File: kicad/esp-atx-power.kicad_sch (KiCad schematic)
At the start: 43 parts, among them J101 Conn_02x02_Odd_Even, J102 Conn_02x02_Odd_Even, J103 Conn_02x02_Odd_Even, J104 Conn_02x02_Odd_Even, J105 GT-USB-7010ASV, K101 G3VM-61D1, K102 G3VM-61D1, K103 G3VM-61D1, K104 G3VM-61D1, Q101 SS8050, Q102 SS8050, SW101 TS-1187A-B-A-B, SW102 TS-1187A-B-A-B, U102 LD1117S33CTR, U103 USBLC6-2P6, U104 CP2102-GMR

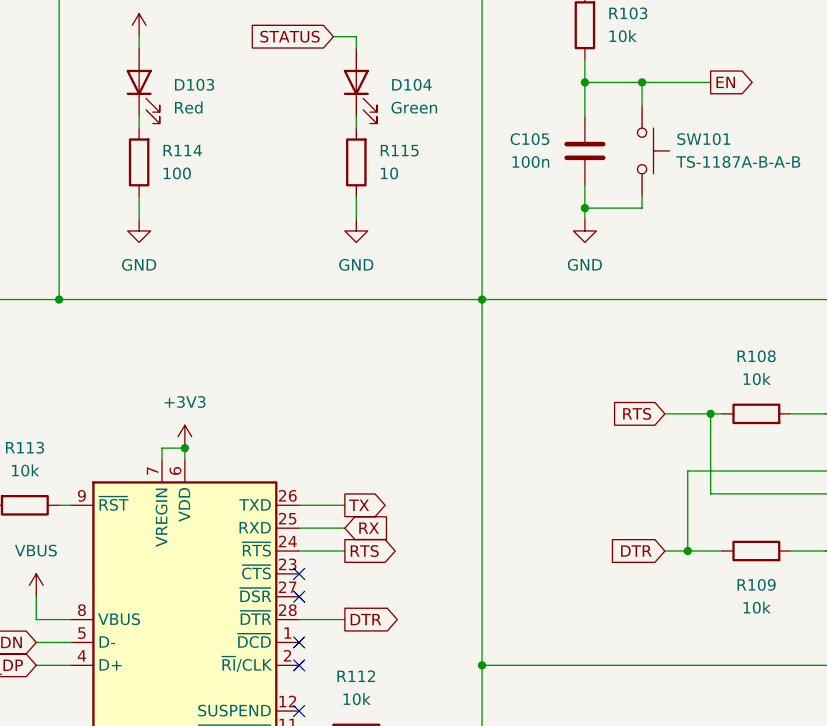
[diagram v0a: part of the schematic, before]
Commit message: Fix RTS/DTR and increase LEDs resistors
- RTS/DTR has been inverted and RTS assertin doesn't reset the board.
- Increase the LED resistors to decrease brightness
- Change JLCPCB order number position
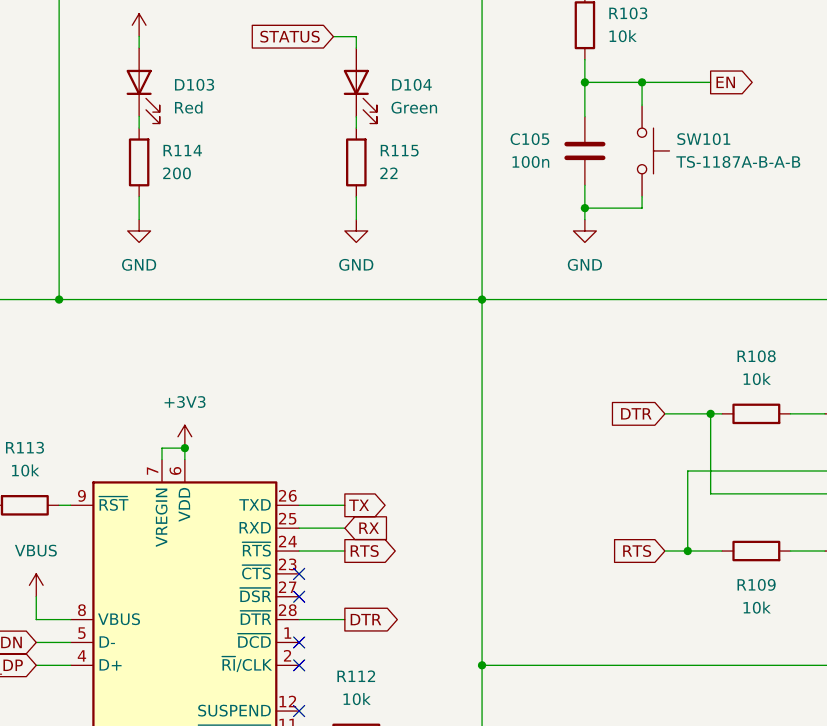
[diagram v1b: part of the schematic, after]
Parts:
- R114: value 100 -> 200; JLCPCB Part# C25076 -> C25087; MFR Part# 0402WGF1000TCE -> 0402WGF2000TCE
- R115: value 10 -> 22; JLCPCB Part# C25077 -> C25092; MFR Part# 0402WGF100JTCE -> 0402WGF220JTCE
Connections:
- net DTR: now also Q102.2 (E), R108.1; no longer Q101.2 (E), R109.1
- net RTS: now also Q101.2 (E), R109.1; no longer Q102.2 (E), R108.1
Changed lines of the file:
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@@
   (title_block
     (title "ESP32 ATX Power Controller")
-    (date "2024-01-14")
-    (rev "1.0.0")
+    (date "2024-02-05")
+    (rev "1.0.1")
   )
   (junction (at 208.28 143.51) (diameter 0) (color 0 0 0 0)
@@
   (junction (at 148.59 33.02) (diameter 0) (color 0 0 0 0)
   )
+  (junction (at 118.11 85.09) (diameter 0) (color 0 0 0 0)
+  )
   (junction (at 62.23 73.66) (diameter 0) (color 0 0 0 0)
   )
@@
   (junction (at 177.8 162.56) (diameter 0) (color 0 0 255 1)
   )
+  (junction (at 119.38 176.53) (diameter 0) (color 0 0 0 0)
+  )
   (junction (at 120.65 69.85) (diameter 0) (color 0 0 0 0)
-  )
-  (junction (at 119.38 176.53) (diameter 0) (color 0 0 0 0)
-  )
-  (junction (at 118.11 85.09) (diameter 0) (color 0 0 0 0)
   )
   (junction (at 209.55 71.12) (diameter 0) (color 0 0 0 0)
@@
     (stroke (width 0) (type default))
   )
+  (wire (pts (xy 115.57 85.09) (xy 118.11 85.09))
+    (stroke (width 0) (type default))
+  )
   (wire (pts (xy 213.36 143.51) (xy 213.36 146.05))
     (stroke (width 0) (type default))
@@
     (stroke (width 0) (type default))
   )
-  (wire (pts (xy 115.57 69.85) (xy 120.65 69.85))
-    (stroke (width 0) (type default))
-  )
   (wire (pts (xy 238.76 92.71) (xy 254 92.71))
     (stroke (width 0) (type default))
@@
   )
   (wire (pts (xy 149.86 176.53) (xy 149.86 179.07))
-    (stroke (width 0) (type default))
-  )
-  (wire (pts (xy 115.57 85.09) (xy 118.11 85.09))
     (stroke (width 0) (type default))
   )
@@
   )
   (wire (pts (xy 207.01 29.21) (xy 215.9 29.21))
+    (stroke (width 0) (type default))
+  )
+  (wire (pts (xy 115.57 69.85) (xy 120.65 69.85))
     (stroke (width 0) (type default))
   )
@@
     )
   )
-  (global_label "RTS" (shape input) (at 115.57 69.85 180) (fields_autoplaced)
+  (global_label "RTS" (shape input) (at 115.57 85.09 180) (fields_autoplaced)
     (effects (font (size 1.27 1.27)) (justify right))
-    (property "Intersheetrefs" "${INTERSHEET_REFS}" (at 109.1377 69.85 0)
+    (property "Intersheetrefs" "${INTERSHEET_REFS}" (at 109.1377 85.09 0)
       (effects (font (size 1.27 1.27)) (justify right) hide)
     )
   )
-  (global_label "DTR" (shape input) (at 115.57 85.09 180) (fields_autoplaced)
+  (global_label "DTR" (shape input) (at 115.57 69.85 180) (fields_autoplaced)
     (effects (font (size 1.27 1.27)) (justify right))
-    (property "Intersheetrefs" "${INTERSHEET_REFS}" (at 109.0772 85.09 0)
+    (property "Intersheetrefs" "${INTERSHEET_REFS}" (at 109.0772 69.85 0)
       (effects (font (size 1.27 1.27)) (justify right) hide)
     )
@@
       (effects (font (size 1.27 1.27)) (justify right))
     )
-    (property "Value" "10" (at 83.82 43.18 0)
+    (property "Value" "22" (at 83.82 43.18 0)
       (effects (font (size 1.27 1.27)) (justify right))
     )
@@
       (effects (font (size 1.27 1.27)) hide)
     )
-    (property "Datasheet" "https://datasheet.lcsc.com/lcsc/2205311900_UNI-ROYAL-Uniroyal-Elec-0402WGF100JTCE_C25077.pdf" (at 81.28 41.91 0)
-      (effects (font (size 1.27 1.27)) hide)
-    )
-    (property "JLCPCB Part#" "C25077" (at 81.28 41.91 90)
+    (property "Datasheet" "https://datasheet.lcsc.com/lcsc/2205311900_UNI-ROYAL-Uniroyal-Elec-0402WGF220JTCE_C25092.pdf" (at 81.28 41.91 0)
+      (effects (font (size 1.27 1.27)) hide)
+    )
+    (property "JLCPCB Part#" "C25092" (at 81.28 41.91 90)
       (effects (font (size 1.27 1.27)) hide)
     )
@@
       (effects (font (size 1.27 1.27)) hide)
     )
-    (property "MFR Part#" "0402WGF100JTCE" (at 81.28 41.91 90)
+    (property "MFR Part#" "0402WGF220JTCE" (at 81.28 41.91 90)
       (effects (font (size 1.27 1.27)) hide)
     )
@@
       (effects (font (size 1.27 1.27)) (justify right))
     )
-    (property "Value" "100" (at 59.69 43.18 0)
+    (property "Value" "200" (at 59.69 43.18 0)
       (effects (font (size 1.27 1.27)) (justify right))
     )
@@
       (effects (font (size 1.27 1.27)) hide)
     )
-    (property "Datasheet" "https://datasheet.lcsc.com/lcsc/2205311900_UNI-ROYAL-Uniroyal-Elec-0402WGF1000TCE_C25076.pdf" (at 57.15 41.91 0)
-      (effects (font (size 1.27 1.27)) hide)
-    )
-    (property "JLCPCB Part#" "C25076" (at 57.15 41.91 90)
+    (property "Datasheet" "https://datasheet.lcsc.com/lcsc/2205311900_UNI-ROYAL-Uniroyal-Elec-0402WGF2000TCE_C25087.pdf" (at 57.15 41.91 0)
+      (effects (font (size 1.27 1.27)) hide)
+    )
+    (property "JLCPCB Part#" "C25087" (at 57.15 41.91 90)
       (effects (font (size 1.27 1.27)) hide)
     )
@@
       (effects (font (size 1.27 1.27)) hide)
     )
-    (property "MFR Part#" "0402WGF1000TCE" (at 57.15 41.91 90)
-      (effects (font (size 1.27 1.27)) hide)
-    )
+    (property "MFR Part#" "0402WGF2000TCE" (at 57.15 41.91 90)
+      (effects (font (size 1.27 1.27)) hide)
+    )

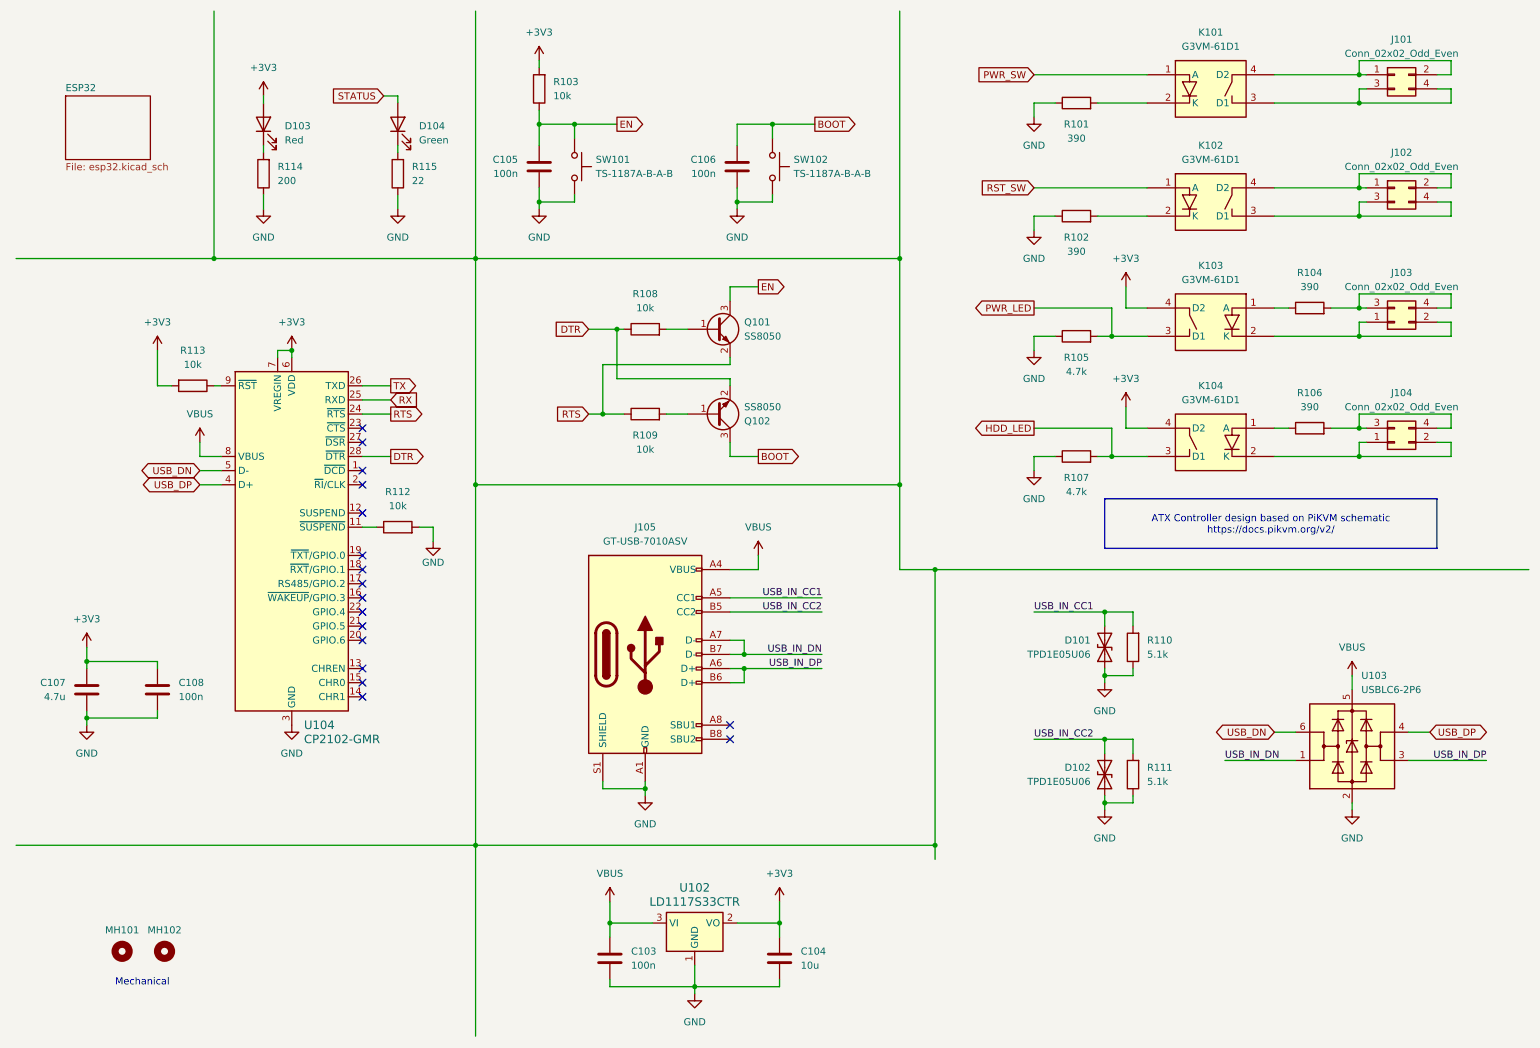
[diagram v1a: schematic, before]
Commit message: Update board form factor and change ESP module
- PCB antenna is not well working inside computer casing
- Select an ESP with external antenna connector
- Remove USB-UART bridge which is no longer required for flashing
- Use on unique pin header instead of 4
- Add 5V external power supply in case USB port is not available
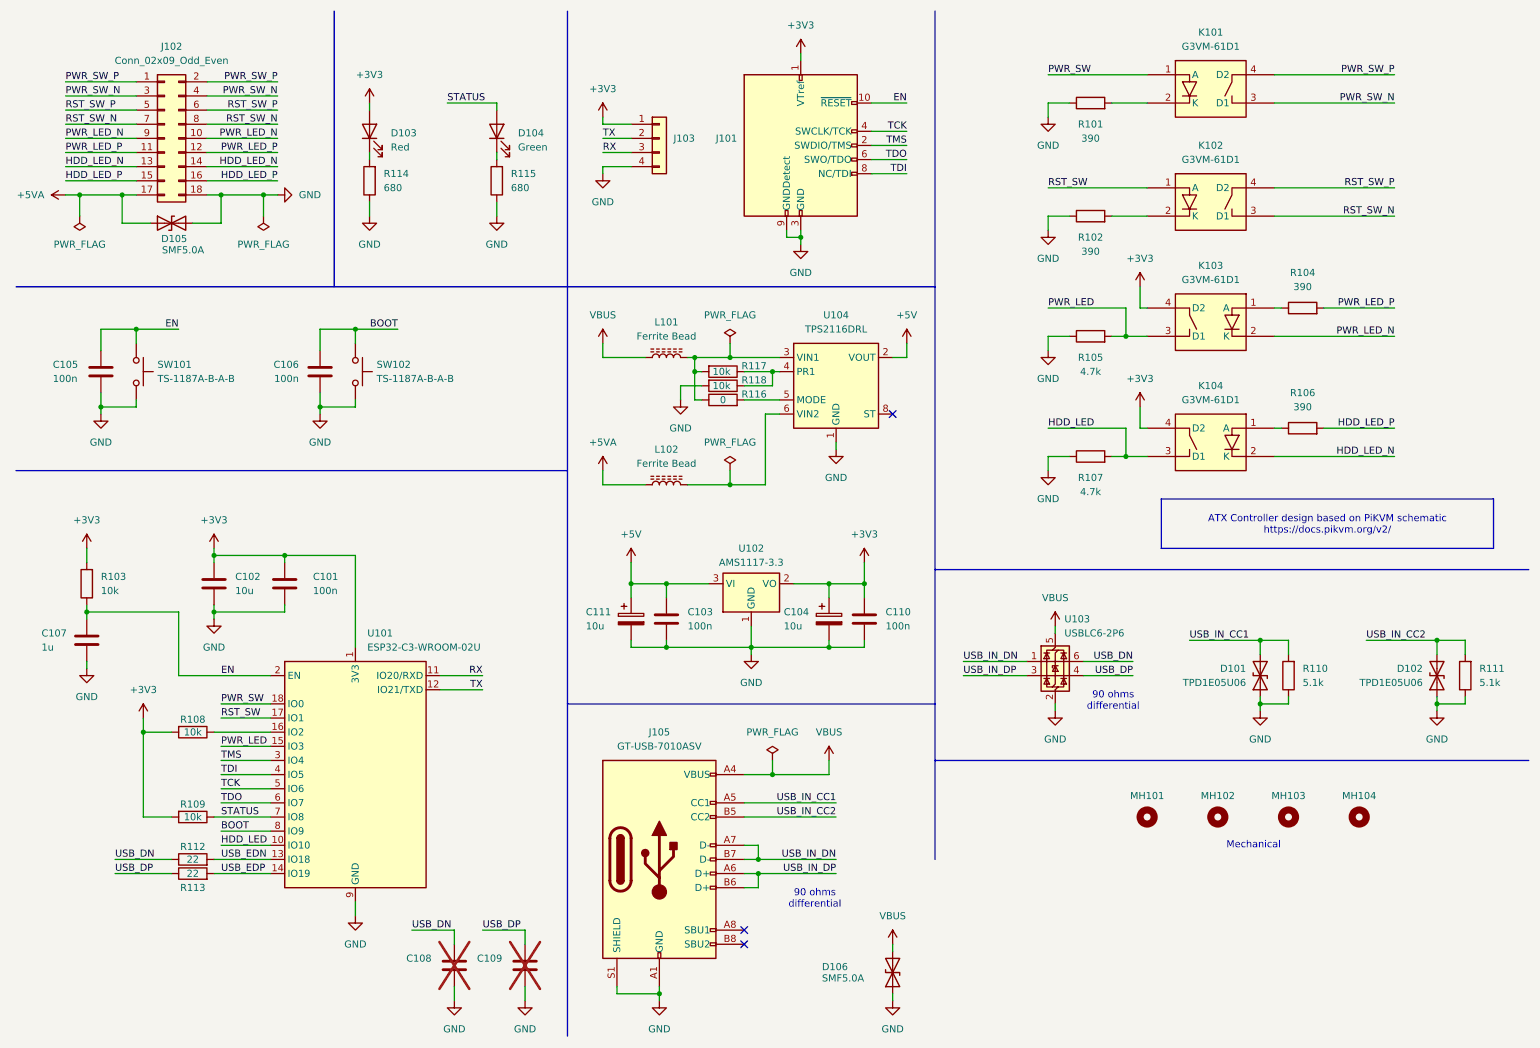
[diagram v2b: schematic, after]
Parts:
- removed J101, J102, J103, J104: Conn_02x02_Odd_Even, Connector_PinHeader_2.54mm:PinHeader_2x02_P2.54mm_Horizontal, symbol Connector_Generic:Conn_02x02_Odd_Even
- removed Q101, Q102: SS8050, Package_TO_SOT_SMD:SOT-23, symbol Device:Q_NPN_BEC
- removed U102: LD1117S33CTR, Package_TO_SOT_SMD:SOT-223-3_TabPin2, symbol Regulator_Linear:LD1117S33TR_SOT223
- removed U104: CP2102-GMR, Package_DFN_QFN:QFN-28-1EP_5x5mm_P0.5mm_EP3.35x3.35mm, symbol Interface_USB:CP2102N-Axx-xQFN28
- added C101: 100n, Capacitor_SMD:C_0402_1005Metric, symbol Device:C
- added C102: 10u, Capacitor_SMD:C_0402_1005Metric, symbol Device:C
- added C109: ~, Capacitor_SMD:C_0402_1005Metric, symbol Device:C
- added C110: 100n, Capacitor_SMD:C_0603_1608Metric, symbol Device:C
- added C111: 10u, Capacitor_Tantalum_SMD:CP_EIA-3216-18_Kemet-A, symbol Device:C_Polarized
- added D105, D106: SMF5.0A, Diode_SMD:D_SOD-123F, symbol Device:D_TVS
- added J101: Conn_ARM_JTAG_SWD_10, Connector_PinHeader_1.27mm:PinHeader_2x05_P1.27mm_Vertical_SMD, symbol Connector:Conn_ARM_JTAG_SWD_10
- added J102: Conn_02x09_Odd_Even, Connector_PinHeader_2.54mm:PinHeader_2x09_P2.54mm_Horizontal, symbol Connector_Generic:Conn_02x09_Odd_Even
- added J103: Conn_01x04, Connector_Molex:Molex_PicoBlade_53261-0471_1x04-1MP_P1.25mm_Horizontal, symbol Connector_Generic:Conn_01x04
- added L101, L102: Ferrite Bead, Inductor_SMD:L_0603_1608Metric, symbol Device:L_Ferrite
- added MH103, MH104: ~, MountingHole:MountingHole_2.7mm_M2.5_ISO7380, symbol Mechanical:MountingHole
- added R116: 0, Resistor_SMD:R_0402_1005Metric, symbol Device:R
- added R117, R118: 10k, Resistor_SMD:R_0402_1005Metric, symbol Device:R
- added U101: ESP32-C3-WROOM-02U, RF_Module:ESP32-C3-WROOM-02U, symbol RF_Module:ESP32-C3-WROOM-02U
- added U102: AMS1117-3.3, Package_TO_SOT_SMD:SOT-223-3_TabPin2, symbol Regulator_Linear:AMS1117-3.3
- added U104: TPS2116DRL, Package_TO_SOT_SMD:SOT-583-8, symbol Power_Management:TPS2116DRL
- C103: footprint Capacitor_SMD:C_0402_1005Metric -> Capacitor_SMD:C_0603_1608Metric; JLCPCB Part# C1525 -> (none); LCSC Part # (none) -> C14663; MFR Part # (none) -> CC0603KRX7R9BB104; MFR Part# CL05B104KO5NNNC -> (none); Manufacturer Samsung Electro-Mechanics -> YAGEO
- C104: footprint Capacitor_SMD:C_0402_1005Metric -> Capacitor_Tantalum_SMD:CP_EIA-3216-18_Kemet-A; symbol Device:C -> Device:C_Polarized; JLCPCB Part# C15525 -> (none); LCSC Part # (none) -> C7171; MFR Part # (none) -> TAJA106K016RNJ; MFR Part# CL05A106MQ5NUNC -> (none); Manufacturer Samsung Electro-Mechanics -> (none)
- C105, C106: JLCPCB Part# C1525 -> (none); LCSC Part # (none) -> C1525; MFR Part # (none) -> CL05B104KO5NNNC; MFR Part# CL05B104KO5NNNC -> (none)
- C107: value 4.7u -> 1u; JLCPCB Part# C23733 -> (none); LCSC Part # (none) -> C52923; MFR Part # (none) -> CL05A105KA5NQNC; MFR Part# CL05A475MP5NRNC -> (none)
- C108: value 100n -> ~; JLCPCB Part# C1525 -> (none); MFR Part# CL05B104KO5NNNC -> (none); Manufacturer Samsung Electro-Mechanics -> (none); now not fitted
- D101, D102: JLCPCB Part# C436349 -> (none); LCSC Part # (none) -> C436349; MFR Part # (none) -> TPD1E05U06DPYR; MFR Part# TPD1E05U06DPYR -> (none)
- D103: footprint LED_SMD:LED_0603_1608Metric -> LED_SMD:LED_0805_2012Metric; JLCPCB Part# C2286 -> (none); LCSC Part # (none) -> C84256; MFR Part # (none) -> NCD0805R1; MFR Part# KT-0603R -> (none); Manufacturer Hubei KENTO Elec -> Foshan NationStar Optoelectronics
- D104: footprint LED_SMD:LED_0603_1608Metric -> LED_SMD:LED_0805_2012Metric; JLCPCB Part# C72043 -> (none); LCSC Part # (none) -> C2297; MFR Part # (none) -> KT-0805G; MFR Part# 19-217/GHC-YR1S2/3T -> (none); Manufacturer Everlight Elec -> Hubei KENTO Elec
- J105: symbol Connector:USB_C_Receptacle_USB2.0 -> Connector:USB_C_Receptacle_USB2.0_16P; JLCPCB Part# C2988369 -> (none); LCSC Part # (none) -> C2988369; MFR Part # (none) -> GT-USB-7010ASV; MFR Part# GT-USB-7010ASV -> (none)
- K101, K102, K103, K104: JLCPCB Part# C469131 -> (none); LCSC Part # (none) -> C469131; MFR Part # (none) -> G3VM-61D1(TR); MFR Part# G3VM-61D1(TR) -> (none)
- R101, R102, R104, R106: JLCPCB Part# C23151 -> (none); LCSC Part # (none) -> C23151; MFR Part # (none) -> 0603WAF3900T5E; MFR Part# 0603WAF3900T5E -> (none)
- R103, R108, R109: JLCPCB Part# C25744 -> (none); LCSC Part # (none) -> C25744; MFR Part # (none) -> 0402WGF1002TCE; MFR Part# 0402WGF1002TCE -> (none)
- R105, R107: JLCPCB Part# C25900 -> (none); LCSC Part # (none) -> C25900; MFR Part # (none) -> 0402WGF4701TCE; MFR Part# 0402WGF4701TCE -> (none)
- R110, R111: JLCPCB Part# C25905 -> (none); LCSC Part # (none) -> C25905; MFR Part # (none) -> 0402WGF5101TCE; MFR Part# 0402WGF5101TCE -> (none)
- R112, R113: value 10k -> 22; JLCPCB Part# C25744 -> (none); LCSC Part # (none) -> C25092; MFR Part # (none) -> 0402WGF220JTCE; MFR Part# 0402WGF1002TCE -> (none)
- R114: value 200 -> 680; JLCPCB Part# C25087 -> (none); LCSC Part # (none) -> C25130; MFR Part # (none) -> 0402WGF6800TCE; MFR Part# 0402WGF2000TCE -> (none)
- R115: value 22 -> 680; JLCPCB Part# C25092 -> (none); LCSC Part # (none) -> C25130; MFR Part # (none) -> 0402WGF6800TCE; MFR Part# 0402WGF220JTCE -> (none)
- SW101, SW102: JLCPCB Part# C318884 -> (none); LCSC Part # (none) -> C318884; MFR Part # (none) -> TS-1187A-B-A-B; MFR Part# TS-1187A-B-A-B -> (none)
- U103: JLCPCB Part# C15999 -> (none); LCSC Part # (none) -> C15999; MFR Part # (none) -> USBLC6-2P6; MFR Part# USBLC6-2P6 -> (none); Manufacturer STMicroelectronics -> STMicroeletronics
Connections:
- net RTS is gone; now on net STATUS: R109.1
- net +3V3: now also R108.2, R109.2, C101.2, C102.1, C110.1, J101.1 (VTref), J103.1 (Pin_1), U101.1 (3V3), U102.2 (VO); no longer C107.1, C108.1, R113.2
- net BOOT: now also U101.8 (IO9)
- net EN: now also C107.1, J101.10 (~{RESET}), U101.2 (EN)
- net GND: now also C101.1, C102.2, C109.2, C110.2, C111.2, D105.2 (A2), D106.1 (A1), J101.3 (GND), J101.5 (GND), J101.9 (GNDDetect), J102.18 (Pin_18), J103.4 (Pin_4), R118.2, U101.19 (GND), U101.9 (GND), U102.1 (GND), U104.1 (GND); no longer R112.2
- net HDD_LED: now also U101.10 (IO10)
- net PWR_LED: now also U101.15 (IO3)
- net PWR_SW: now also U101.18 (IO0)
- net RST_SW: now also U101.17 (IO1)
- net RX: now also J103.3 (Pin_3), U101.11 (IO20/RXD)
- net STATUS: now also U101.7 (IO8)
- net TX: now also J103.2 (Pin_2), U101.12 (IO21/TXD)
- net USB_DN: now also C108.1, R112.1
- net USB_DP: now also R113.1, C109.1
- net VBUS: now also D106.2 (A2), L101.1; no longer C103.1
- net PWR_LED_N: now reaches K103.2 (K)
- net PWR_LED_N: now also J102.10 (Pin_10), J102.9 (Pin_9)
- net PWR_LED_P: now reaches R104.2
- net PWR_LED_P: now also J102.11 (Pin_11), J102.12 (Pin_12)
- net PWR_SW_P: now reaches K101.4 (D2)
- net PWR_SW_P: now also J102.1 (Pin_1), J102.2 (Pin_2)
- net PWR_SW_N: now reaches K101.3 (D1)
- net PWR_SW_N: now also J102.3 (Pin_3), J102.4 (Pin_4)
- net HDD_LED_P: now reaches R106.2
- net HDD_LED_P: now also J102.15 (Pin_15), J102.16 (Pin_16)
- net RST_SW_N: now reaches K102.3 (D1)
- net RST_SW_N: now also J102.7 (Pin_7), J102.8 (Pin_8)
- net RST_SW_P: now reaches K102.4 (D2)
- net RST_SW_P: now also J102.5 (Pin_5), J102.6 (Pin_6)
- net HDD_LED_N: now reaches K104.2 (K)
- net HDD_LED_N: now also J102.13 (Pin_13), J102.14 (Pin_14)
- net DTR: no longer names the net of R108.1
- net DTR: now also U101.16 (IO2)
- new net: L102.2, U104.6 (VIN2)
- new net: L101.2, R116.1, R117.2, U104.3 (VIN1)
- new net: R117.1, R118.1, U104.4 (PR1)
- new net: R116.2, U104.5 (MODE)
- new net +5V: C103.1, C111.1, U102.3 (VI), U104.2 (VOUT), U104.7 (VOUT)
- new net +5VA: D105.1 (A1), J102.17 (Pin_17), L102.1
- new net TCK: J101.4 (SWCLK/TCK), U101.5 (IO6)
- new net TDI: J101.8 (NC/TDI), U101.4 (IO5)
- new net TDO: J101.6 (SWO/TDO), U101.6 (IO7)
- new net TMS: J101.2 (SWDIO/TMS), U101.3 (IO4)
- new net USB_EDN: R112.2, U101.13 (IO18)
- new net USB_EDP: R113.2, U101.14 (IO19)
- no-connect marks 17 -> 3
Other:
- removed sheet ESP32
- note added: "90 ohms differential"
- moved on the sheet: C103, C106, D101, D102, D103, D104, J105, MH101, MH102, R101, R102, R103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
